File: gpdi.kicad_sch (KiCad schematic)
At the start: 21 parts, among them U11 PCA9306D

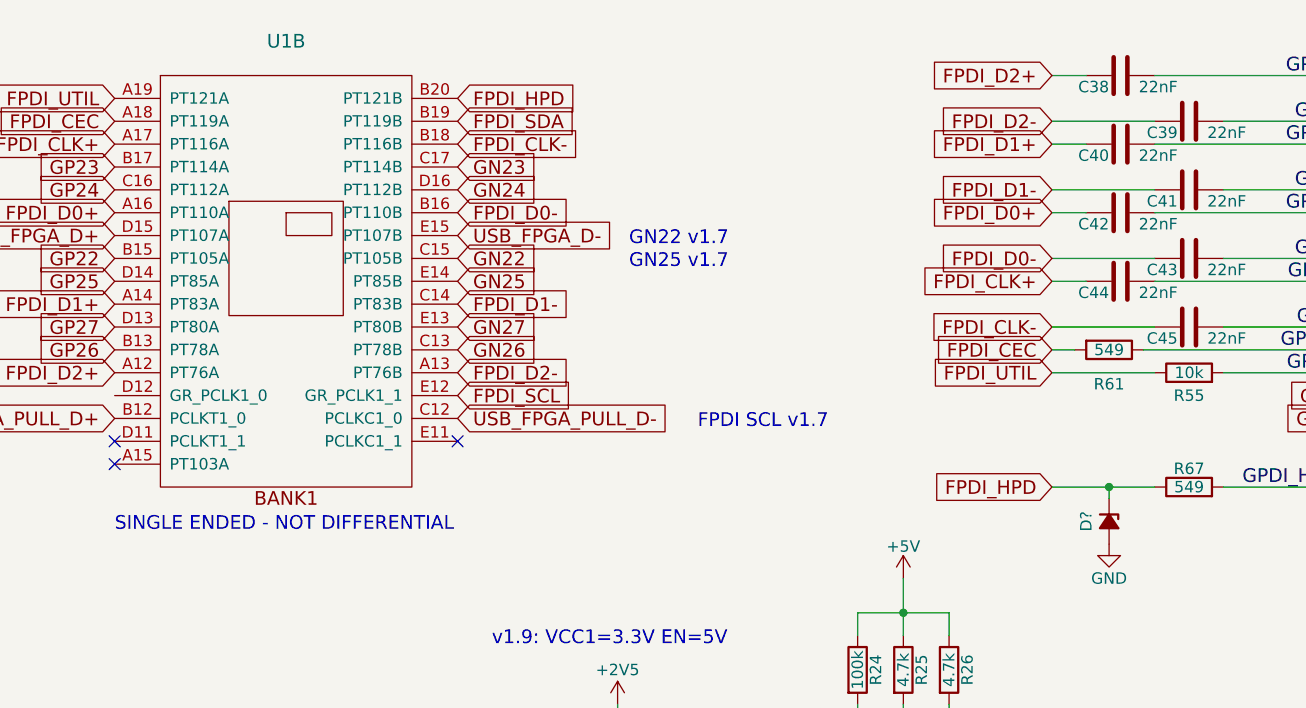
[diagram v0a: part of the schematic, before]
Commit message: Full SerDes is now connected
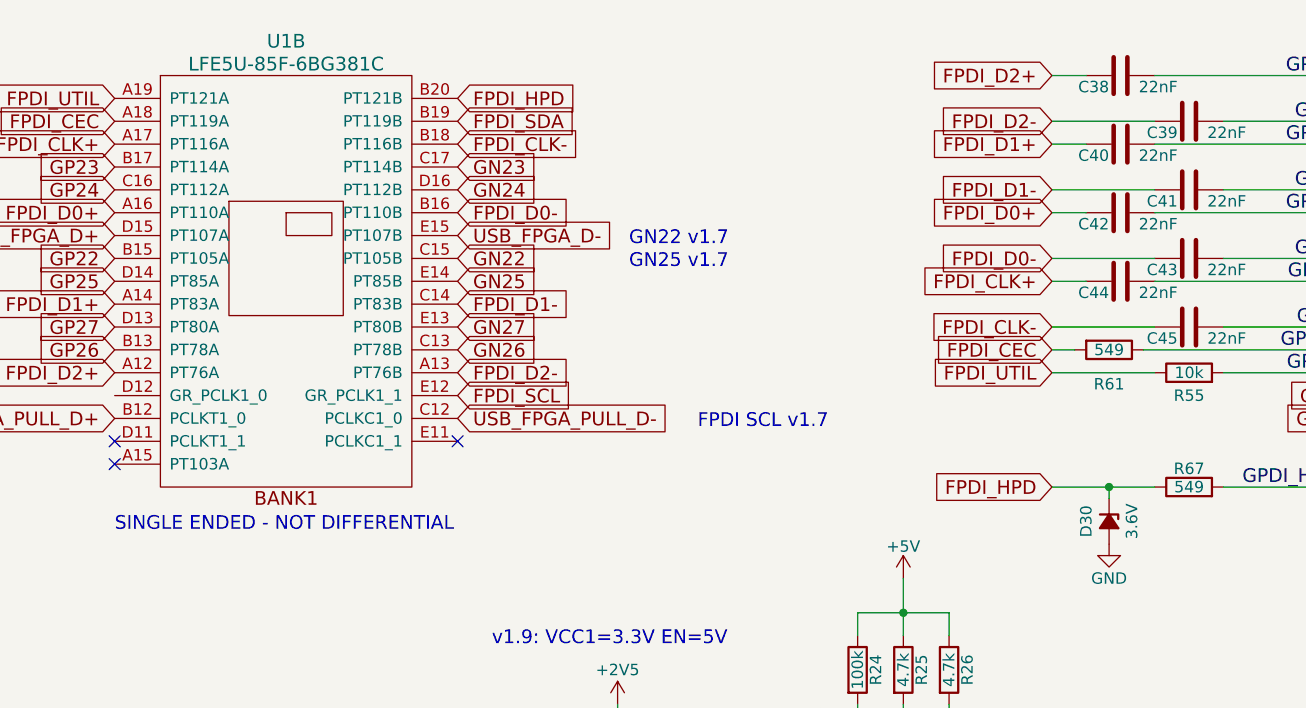
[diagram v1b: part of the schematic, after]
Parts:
- D30: renamed from D?; value (none) -> 3.6V; footprint (none) -> Diode_SMD:D_SOD-323_HandSoldering
- U1: value (none) -> LFE5U-85F-6BG381C; footprint (none) -> lfe5bg381:BGA-381_pitch0.8mm_dia0.4mm; MNF1_URL (none) -> www.latticesemi.com; Mouser_URL www.mouser.com -> (none)
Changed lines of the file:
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@@
   )
   (symbol (lib_id "lfe5bg381:LFE5UM-85F-6BG381C") (at 91.44 73.66 0) (unit 2)
-    (in_bom yes) (on_board yes)
+    (in_bom yes) (on_board no)
     (property "Reference" "U1" (id 0) (at 91.44 49.53 0)
       (effects (font (size 1.524 1.524)))
     )
-    (property "Value" "" (id 1) (at 91.44 52.07 0)
+    (property "Value" "LFE5U-85F-6BG381C" (id 1) (at 91.44 52.07 0)
       (effects (font (size 1.524 1.524)))
     )
-    (property "Footprint" "" (id 2) (at 64.77 49.53 0)
+    (property "Footprint" "lfe5bg381:BGA-381_pitch0.8mm_dia0.4mm" (id 2) (at 64.77 49.53 0)
       (effects (font (size 1.524 1.524)) hide)
     )
-    (property "Datasheet" "http://www.latticesemi.com/~/media/LatticeSemi/Documents/DataSheets/ECP5/FPGA-DS-02012.pdf" (id 3) (at 64.77 49.53 0)
+    (property "Datasheet" "http://www.latticesemi.com/~/media/LatticeSemi/Documents/ApplicationNotes/EH/TN1261.pdf?document_id=50463" (id 3) (at 64.77 49.53 0)
       (effects (font (size 1.524 1.524)) hide)
     )
@@
       (effects (font (size 1.524 1.524)) hide)
     )
-    (property "Mouser_URL" "www.mouser.com" (id 5) (at 91.44 73.66 0)
+    (property "MNF1_URL" "www.latticesemi.com" (id 5) (at 91.44 73.66 0)
       (effects (font (size 1.524 1.524)) hide)
     )
@@
   (symbol (lib_id "ulx3s-rescue:D_Zener_Small_ALT-Device") (at 182.88 102.87 270) (unit 1)
     (in_bom yes) (on_board yes)
-    (property "Reference" "D?" (id 0) (at 180.34 102.87 0))
-    (property "Value" "" (id 1) (at 185.42 102.87 0))
-    (property "Footprint" "" (id 2) (at 182.88 102.87 90)
-      (effects (font (size 1.27 1.27)) hide)
-    )
+    (property "Reference" "D30" (id 0) (at 180.34 102.87 0))
+    (property "Value" "3.6V" (id 1) (at 185.42 102.87 0))
+    (property "Footprint" "Diode_SMD:D_SOD-323_HandSoldering" (id 2) (at 182.88 102.87 90)
+      (effects (font (size 1.27 1.27)) hide)
+    )
